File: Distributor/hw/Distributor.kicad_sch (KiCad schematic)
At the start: 23 parts, among them J1 Conn_01x04, J100 Conn_01x03, J2 Conn_01x06_MountingPin, U1 SPX3819M5-L-3-3, U2 STM32G030C8Tx, U3 SN74AHCT245PWR, U4 SN74AHCT245PWR, U5 SN74AHCT245PWR, U6 SN74AHCT245PWR

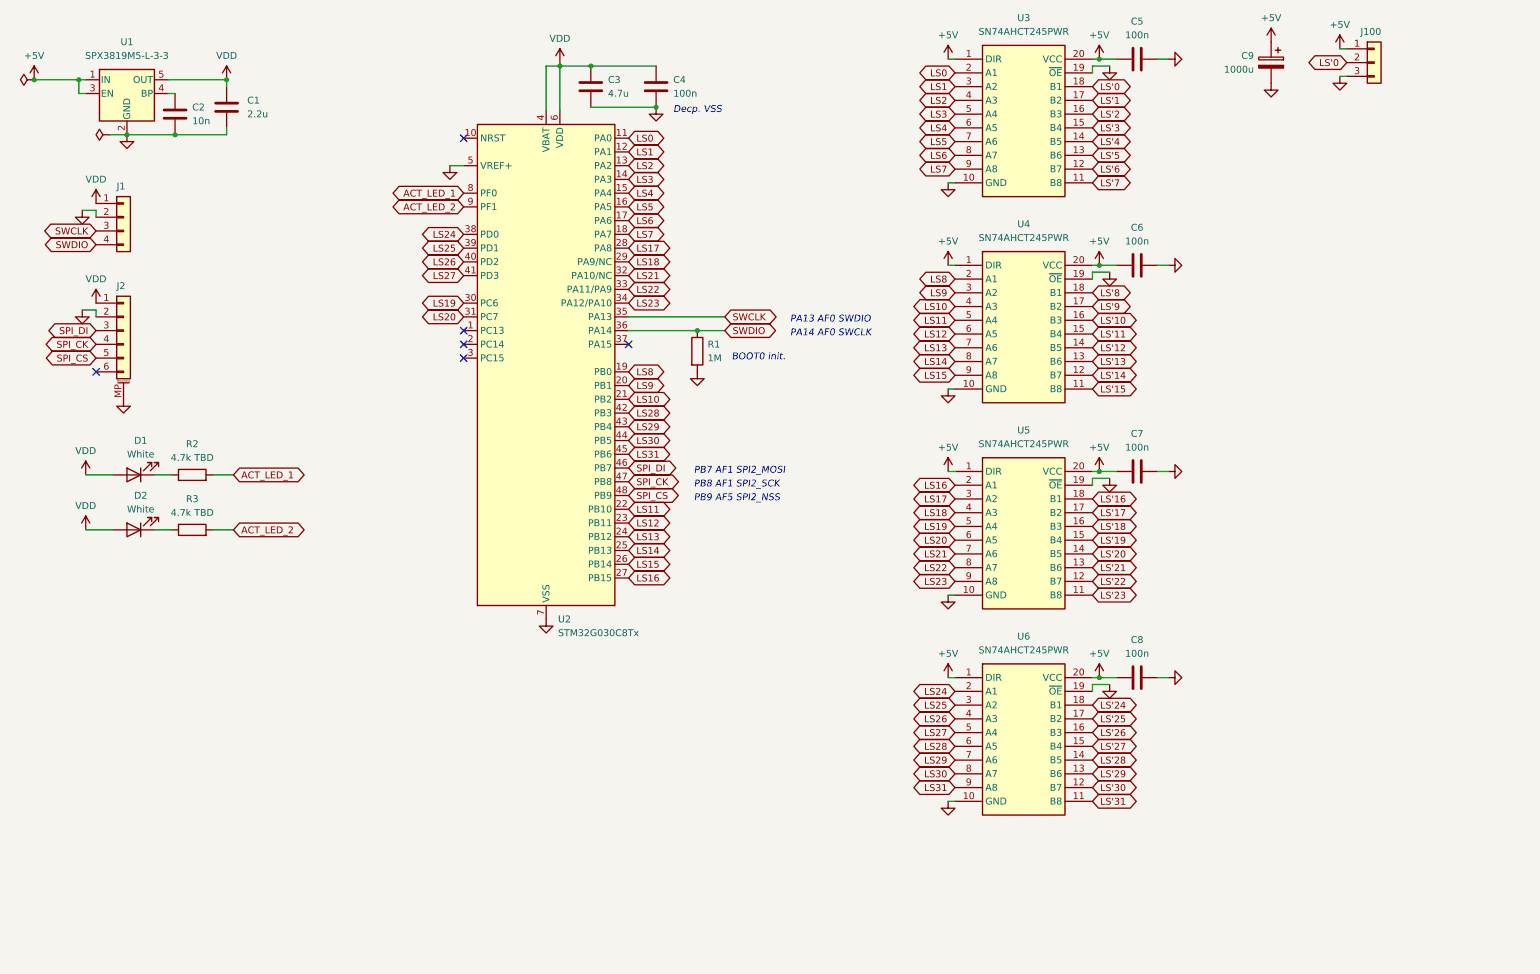
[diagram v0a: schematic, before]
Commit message: Merge distributor and grabber schematic into one
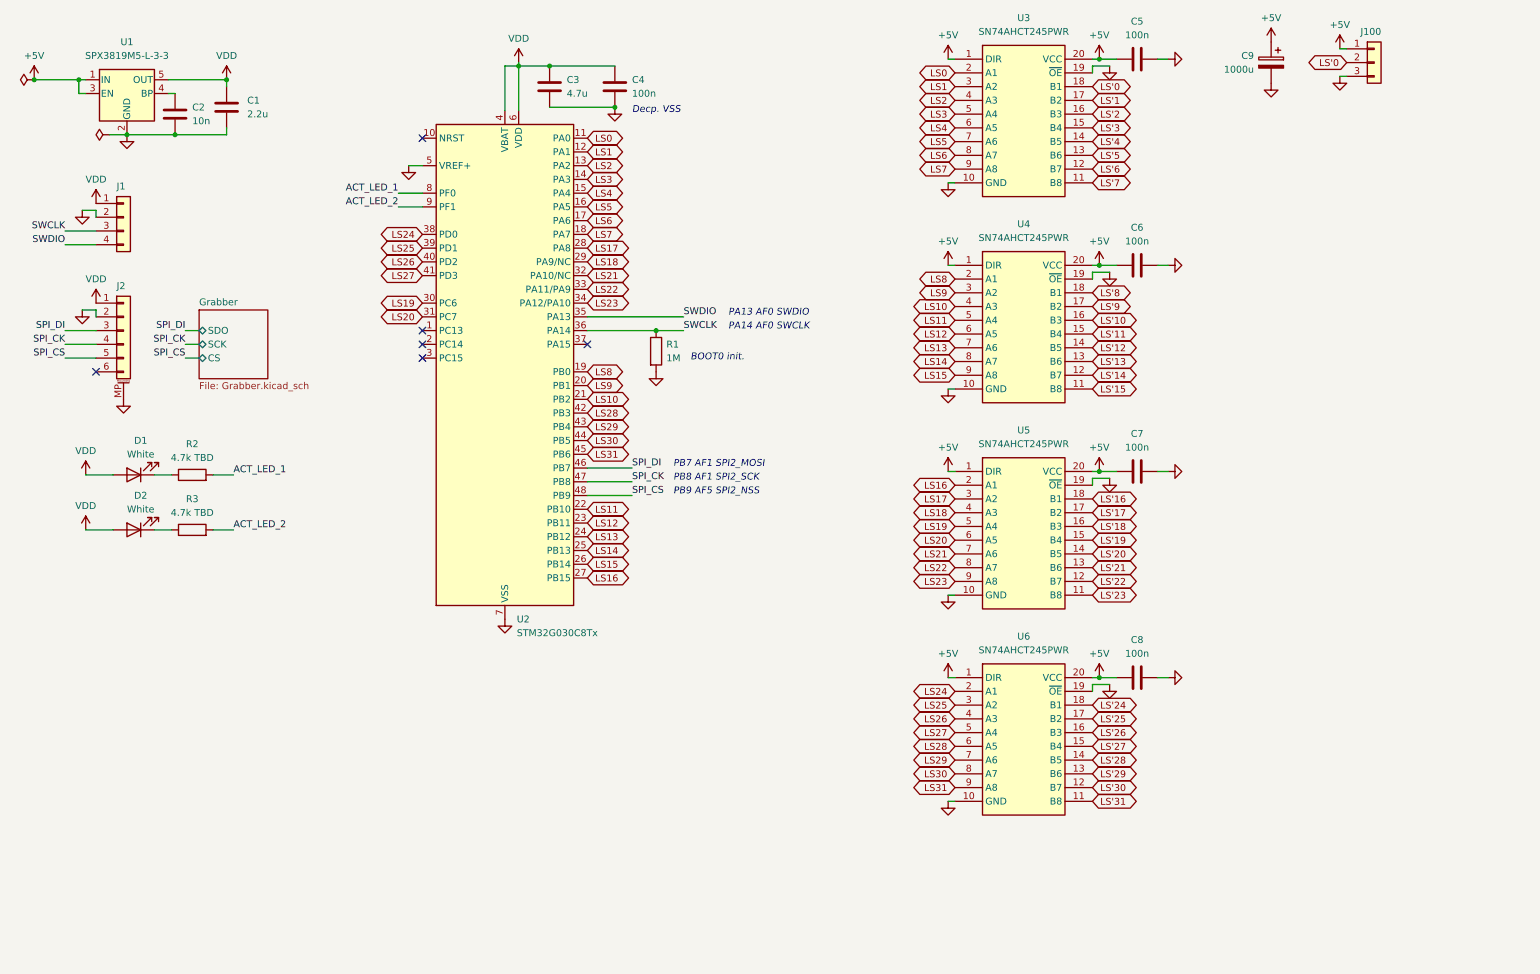
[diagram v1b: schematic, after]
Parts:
- J100: footprint (none) -> Connector_PinHeader_2.54mm:PinHeader_1x03_P2.54mm_Vertical
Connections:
- net SWCLK: now also R1.1, U2.36 (PA14); no longer U2.35 (PA13)
- net SWDIO: now also U2.35 (PA13); no longer R1.1, U2.36 (PA14)
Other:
- added sheet Grabber (Grabber.kicad_sch)
- moved on the sheet: C3, C4, R1, U2

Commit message: Add MLX90640 sensor to schematic
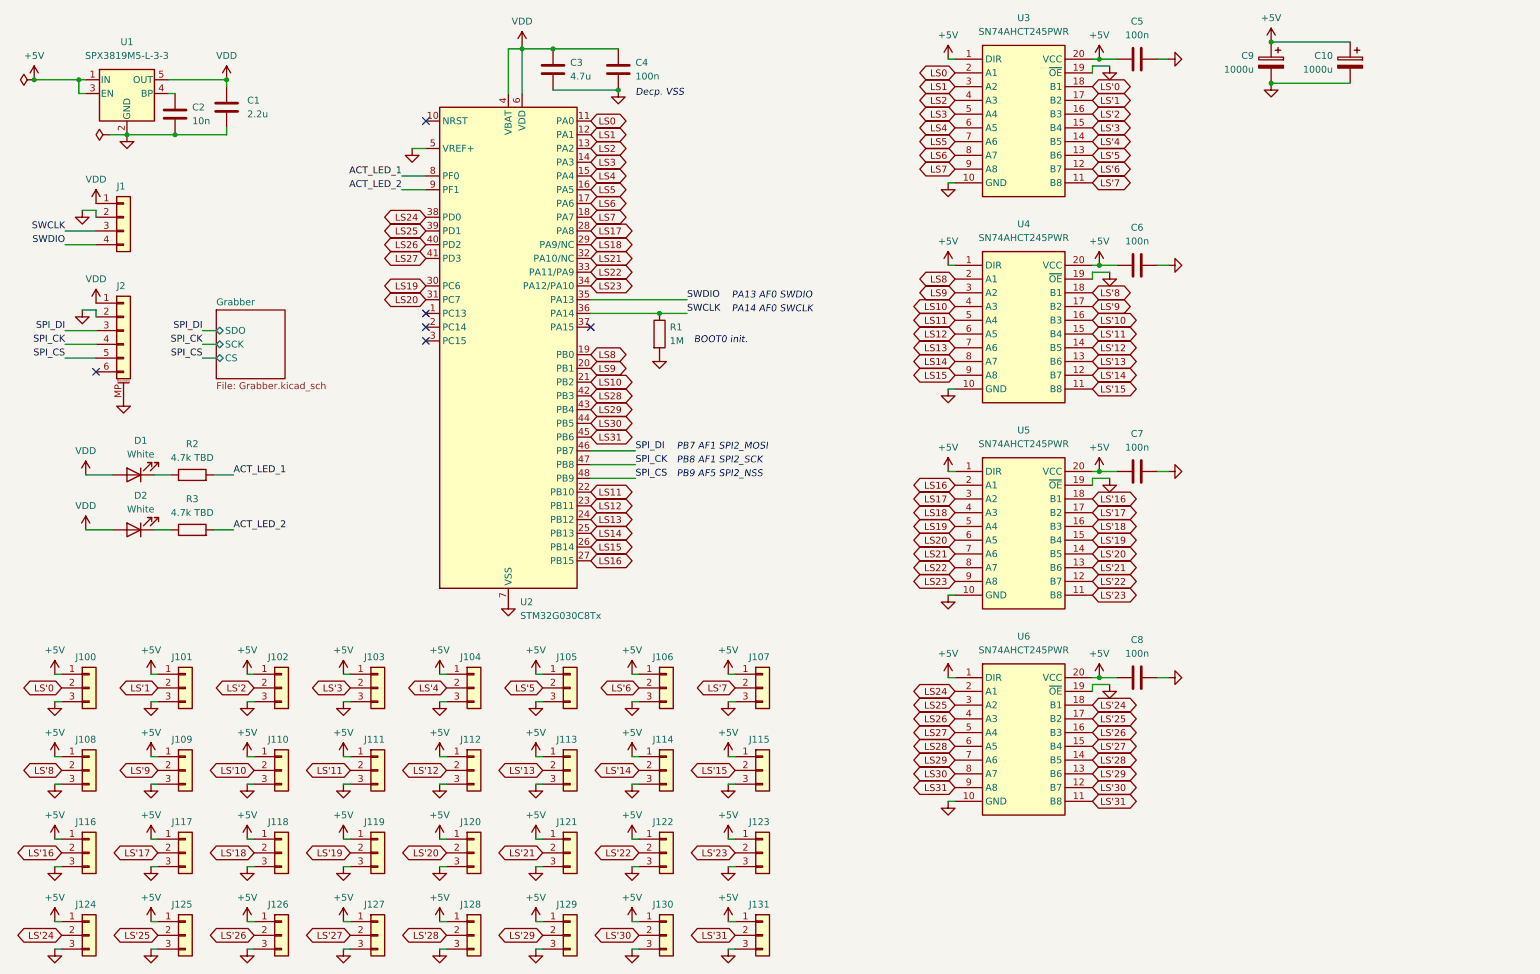
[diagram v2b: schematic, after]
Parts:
- added C10: 1000u, Capacitor_SMD:CP_Elec_8x10.5, symbol Device:C_Polarized
- added J101, J102, J103, J104, J105, J106, J107, J108, J109, J110, J111, J112, J113, J114, J115, J116, J117, J118, J119, J120, J121, J122, J123, J124, J125, J126, J127, J128, J129, J130, J131: Conn_01x03, Distributor_footprints:PinHeader_1x03_P2.54mm_Vertical, symbol Connector_Generic:Conn_01x03
- J100: footprint Connector_PinHeader_2.54mm:PinHeader_1x03_P2.54mm_Vertical -> Distributor_footprints:PinHeader_1x03_P2.54mm_Vertical
- J2: footprint Connector_FFC-FPC:TE_84952-6_1x06-1MP_P1.0mm_Horizontal -> Connector_FFC-FPC:Jushuo_AFC07-S06FCA-00_1x6-1MP_P0.50_Horizontal
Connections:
- net +5V: now also C10.1, J101.1 (Pin_1), J102.1 (Pin_1), J103.1 (Pin_1), J104.1 (Pin_1), J105.1 (Pin_1), J106.1 (Pin_1), J107.1 (Pin_1), J108.1 (Pin_1), J109.1 (Pin_1), J110.1 (Pin_1), J111.1 (Pin_1), J112.1 (Pin_1), J113.1 (Pin_1), J114.1 (Pin_1), J115.1 (Pin_1), J116.1 (Pin_1), J117.1 (Pin_1), J118.1 (Pin_1), J119.1 (Pin_1), J120.1 (Pin_1), J121.1 (Pin_1), J122.1 (Pin_1), J123.1 (Pin_1), J124.1 (Pin_1), J125.1 (Pin_1), J126.1 (Pin_1), J127.1 (Pin_1), J128.1 (Pin_1), J129.1 (Pin_1), J130.1 (Pin_1), J131.1 (Pin_1)
- net GND: now also C10.2, J101.3 (Pin_3), J102.3 (Pin_3), J103.3 (Pin_3), J104.3 (Pin_3), J105.3 (Pin_3), J106.3 (Pin_3), J107.3 (Pin_3), J108.3 (Pin_3), J109.3 (Pin_3), J110.3 (Pin_3), J111.3 (Pin_3), J112.3 (Pin_3), J113.3 (Pin_3), J114.3 (Pin_3), J115.3 (Pin_3), J116.3 (Pin_3), J117.3 (Pin_3), J118.3 (Pin_3), J119.3 (Pin_3), J120.3 (Pin_3), J121.3 (Pin_3), J122.3 (Pin_3), J123.3 (Pin_3), J124.3 (Pin_3), J125.3 (Pin_3), J126.3 (Pin_3), J127.3 (Pin_3), J128.3 (Pin_3), J129.3 (Pin_3), J130.3 (Pin_3), J131.3 (Pin_3)
- net LS'1: now also J101.2 (Pin_2)
- net LS'10: now also J110.2 (Pin_2)
- net LS'11: now also J111.2 (Pin_2)
- net LS'12: now also J112.2 (Pin_2)
- net LS'13: now also J113.2 (Pin_2)
- net LS'14: now also J114.2 (Pin_2)
- net LS'15: now also J115.2 (Pin_2)
- net LS'16: now also J116.2 (Pin_2)
- net LS'17: now also J117.2 (Pin_2)
- net LS'18: now also J118.2 (Pin_2)
- net LS'19: now also J119.2 (Pin_2)
- net LS'2: now also J102.2 (Pin_2)
- net LS'20: now also J120.2 (Pin_2)
- net LS'21: now also J121.2 (Pin_2)
- net LS'22: now also J122.2 (Pin_2)
- net LS'23: now also J123.2 (Pin_2)
- net LS'24: now also J124.2 (Pin_2)
- net LS'25: now also J125.2 (Pin_2)
- net LS'26: now also J126.2 (Pin_2)
- net LS'27: now also J127.2 (Pin_2)
- net LS'28: now also J128.2 (Pin_2)
- net LS'29: now also J129.2 (Pin_2)
- net LS'3: now also J103.2 (Pin_2)
- net LS'30: now also J130.2 (Pin_2)
- net LS'31: now also J131.2 (Pin_2)
- net LS'4: now also J104.2 (Pin_2)
- net LS'5: now also J105.2 (Pin_2)
- net LS'6: now also J106.2 (Pin_2)
- net LS'7: now also J107.2 (Pin_2)
- net LS'8: now also J108.2 (Pin_2)
- net LS'9: now also J109.2 (Pin_2)
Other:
- moved on the sheet: C3, C4, J100, R1, U2

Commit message: Separate 5V power supplies into four domains
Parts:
- added C11, C12: 1000u, Capacitor_SMD:CP_Elec_8x10.5, symbol Device:C_Polarized
- added J3, J4, J5, J6: Conn_01x02, Connector_PinHeader_2.54mm:PinHeader_1x02_P2.54mm_Vertical, symbol Connector_Generic:Conn_01x02
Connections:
- net GND: now also C11.2, C12.2, J3.2 (Pin_2), J4.2 (Pin_2), J5.2 (Pin_2), J6.2 (Pin_2)
- net LS'0: now also U3.11 (B8); no longer U3.18 (B1)
- net LS'1: now also U3.12 (B7); no longer U3.17 (B2)
- net LS'10: now also U4.13 (B6); no longer U4.16 (B3)
- net LS'11: now also U4.14 (B5); no longer U4.15 (B4)
- net LS'12: now also U4.15 (B4); no longer U4.14 (B5)
- net LS'13: now also U4.16 (B3); no longer U4.13 (B6)
- net LS'14: now also U4.17 (B2); no longer U4.12 (B7)
- net LS'15: now also U4.18 (B1); no longer U4.11 (B8)
- net LS'16: now also U5.11 (B8); no longer U5.18 (B1)
- net LS'17: now also U5.12 (B7); no longer U5.17 (B2)
- net LS'18: now also U5.13 (B6); no longer U5.16 (B3)
- net LS'19: now also U5.14 (B5); no longer U5.15 (B4)
- net LS'2: now also U3.13 (B6); no longer U3.16 (B3)
- net LS'20: now also U5.15 (B4); no longer U5.14 (B5)
- net LS'21: now also U5.16 (B3); no longer U5.13 (B6)
- net LS'22: now also U5.17 (B2); no longer U5.12 (B7)
- net LS'23: now also U5.18 (B1); no longer U5.11 (B8)
- net LS'24: now also U6.11 (B8); no longer U6.18 (B1)
- net LS'25: now also U6.12 (B7); no longer U6.17 (B2)
- net LS'26: now also U6.13 (B6); no longer U6.16 (B3)
- net LS'27: now also U6.14 (B5); no longer U6.15 (B4)
- net LS'28: now also U6.15 (B4); no longer U6.14 (B5)
- net LS'29: now also U6.16 (B3); no longer U6.13 (B6)
- net LS'3: now also U3.14 (B5); no longer U3.15 (B4)
- net LS'30: now also U6.17 (B2); no longer U6.12 (B7)
- net LS'31: now also U6.18 (B1); no longer U6.11 (B8)
- net LS'4: now also U3.15 (B4); no longer U3.14 (B5)
- net LS'5: now also U3.16 (B3); no longer U3.13 (B6)
- net LS'6: now also U3.17 (B2); no longer U3.12 (B7)
- net LS'7: now also U3.18 (B1); no longer U3.11 (B8)
- net LS'8: now also U4.11 (B8); no longer U4.18 (B1)
- net LS'9: now also U4.12 (B7); no longer U4.17 (B2)
- net LS0: now also U3.9 (A8); no longer U3.2 (A1)
- net LS1: now also U3.8 (A7); no longer U3.3 (A2)
- net LS10: now also U4.7 (A6); no longer U4.4 (A3)
- net LS11: now also U4.6 (A5); no longer U4.5 (A4)
- net LS12: now also U4.5 (A4); no longer U4.6 (A5)
- net LS13: now also U4.4 (A3); no longer U4.7 (A6)
- net LS14: now also U4.3 (A2); no longer U4.8 (A7)
- net LS15: now also U4.2 (A1); no longer U4.9 (A8)
- net LS16: now also U5.9 (A8); no longer U5.2 (A1)
- net LS17: now also U5.8 (A7); no longer U5.3 (A2)
- net LS18: now also U5.7 (A6); no longer U5.4 (A3)
- net LS19: now also U5.6 (A5); no longer U5.5 (A4)
- net LS2: now also U3.7 (A6); no longer U3.4 (A3)
- net LS20: now also U5.5 (A4); no longer U5.6 (A5)
- net LS21: now also U5.4 (A3); no longer U5.7 (A6)
- net LS22: now also U5.3 (A2); no longer U5.8 (A7)
- net LS23: now also U5.2 (A1); no longer U5.9 (A8)
- net LS24: now also U6.9 (A8); no longer U6.2 (A1)
- net LS25: now also U6.8 (A7); no longer U6.3 (A2)
- net LS26: now also U6.7 (A6); no longer U6.4 (A3)
- net LS27: now also U6.6 (A5); no longer U6.5 (A4)
- net LS28: now also U6.5 (A4); no longer U6.6 (A5)
- net LS29: now also U6.4 (A3); no longer U6.7 (A6)
- net LS3: now also U3.6 (A5); no longer U3.5 (A4)
- net LS30: now also U6.3 (A2); no longer U6.8 (A7)
- net LS31: now also U6.2 (A1); no longer U6.9 (A8)
- net LS4: now also U3.5 (A4); no longer U3.6 (A5)
- net LS5: now also U3.4 (A3); no longer U3.7 (A6)
- net LS6: now also U3.3 (A2); no longer U3.8 (A7)
- net LS7: now also U3.2 (A1); no longer U3.9 (A8)
- net LS8: now also U4.9 (A8); no longer U4.2 (A1)
- net LS9: now also U4.8 (A7); no longer U4.3 (A2)
- removed net +5V: C10.1, C5.1, C6.1, C7.1, C8.1, C9.1, J100.1 (Pin_1), J101.1 (Pin_1), J102.1 (Pin_1), J103.1 (Pin_1), J104.1 (Pin_1), J105.1 (Pin_1), J106.1 (Pin_1), J107.1 (Pin_1), J108.1 (Pin_1), J109.1 (Pin_1), J110.1 (Pin_1), J111.1 (Pin_1), J112.1 (Pin_1), J113.1 (Pin_1), J114.1 (Pin_1), J115.1 (Pin_1), J116.1 (Pin_1), J117.1 (Pin_1), J118.1 (Pin_1), J119.1 (Pin_1), J120.1 (Pin_1), J121.1 (Pin_1), J122.1 (Pin_1), J123.1 (Pin_1), J124.1 (Pin_1), J125.1 (Pin_1), J126.1 (Pin_1), J127.1 (Pin_1), J128.1 (Pin_1), J129.1 (Pin_1), J130.1 (Pin_1), J131.1 (Pin_1), U1.1 (IN), U1.3 (EN), U3.1 (DIR), U3.20 (VCC), U4.1 (DIR), U4.20 (VCC), U5.1 (DIR), U5.20 (VCC), U6.1 (DIR), U6.20 (VCC)
- new net +5V-A: C5.1, C9.1, J100.1 (Pin_1), J101.1 (Pin_1), J102.1 (Pin_1), J103.1 (Pin_1), J104.1 (Pin_1), J105.1 (Pin_1), J106.1 (Pin_1), J107.1 (Pin_1), J3.1 (Pin_1), U3.1 (DIR), U3.20 (VCC)
- new net +5V-B: C10.1, C6.1, J108.1 (Pin_1), J109.1 (Pin_1), J110.1 (Pin_1), J111.1 (Pin_1), J112.1 (Pin_1), J113.1 (Pin_1), J114.1 (Pin_1), J115.1 (Pin_1), J4.1 (Pin_1), U4.1 (DIR), U4.20 (VCC)
- new net +5V-C: C11.1, C7.1, J116.1 (Pin_1), J117.1 (Pin_1), J118.1 (Pin_1), J119.1 (Pin_1), J120.1 (Pin_1), J121.1 (Pin_1), J122.1 (Pin_1), J123.1 (Pin_1), J5.1 (Pin_1), U5.1 (DIR), U5.20 (VCC)
- new net +5V-D: C12.1, C8.1, J124.1 (Pin_1), J125.1 (Pin_1), J126.1 (Pin_1), J127.1 (Pin_1), J128.1 (Pin_1), J129.1 (Pin_1), J130.1 (Pin_1), J131.1 (Pin_1), J6.1 (Pin_1), U1.1 (IN), U1.3 (EN), U6.1 (DIR), U6.20 (VCC)

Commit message: Board layout
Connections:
- net +5V-A: now also U1.1 (IN), U1.3 (EN)
- net +5V-D: no longer U1.1 (IN), U1.3 (EN)
- net GND: no longer U2.5 (VREF+)
- net VDD: now also U2.5 (VREF+)
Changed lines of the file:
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@@
     (stroke (width 0) (type default))
   )
-  (wire (pts (xy 93.98 40.005) (xy 96.52 40.005))
+  (wire (pts (xy 92.71 40.005) (xy 96.52 40.005))
     (stroke (width 0) (type default))
   )
@@
     )
   )
-  (symbol (lib_id "Distributor_symbols:+5V-D") (at 24.13 27.305 0) (unit 1)
-    (in_bom yes) (on_board yes) (dnp no)
-    (property "Reference" "#PWR01" (at 24.13 31.115 0)
-      (effects (font (size 1.27 1.27)) hide)
-    )
-    (property "Value" "+5V-D" (at 24.13 22.86 0)
-      (effects (font (size 1.27 1.27)))
-    )
-    (property "Footprint" "" (at 24.13 27.305 0)
-      (effects (font (size 1.27 1.27)) hide)
-    )
-    (property "Datasheet" "" (at 24.13 27.305 0)
-      (effects (font (size 1.27 1.27)) hide)
-    )
-    (pin "1")
-    (instances
-      (project "Distributor"
-        (path "/3f67d80a-1b5b-4b57-a63e-46eb7de4787a"
-          (reference "#PWR01") (unit 1)
-        )
-      )
-    )
-  )
   (symbol (lib_id "power:GND") (at 278.13 43.815 0) (unit 1)
     (in_bom yes) (on_board yes) (dnp no) (fields_autoplaced)
@@
     )
   )
-  (symbol (lib_id "power:GND") (at 93.98 40.005 0) (unit 1)
-    (in_bom yes) (on_board yes) (dnp no) (fields_autoplaced)
-    (property "Reference" "#PWR09" (at 93.98 46.355 0)
-      (effects (font (size 1.27 1.27)) hide)
-    )
-    (property "Value" "GND" (at 93.98 44.45 0)
-      (effects (font (size 1.27 1.27)) hide)
-    )
-    (property "Footprint" "" (at 93.98 40.005 0)
-      (effects (font (size 1.27 1.27)) hide)
-    )
-    (property "Datasheet" "" (at 93.98 40.005 0)
-      (effects (font (size 1.27 1.27)) hide)
-    )
-    (pin "1")
-    (instances
-      (project "Distributor"
-        (path "/3f67d80a-1b5b-4b57-a63e-46eb7de4787a"
-          (reference "#PWR09") (unit 1)
-        )
-      )
-    )
-  )
   (symbol (lib_id "Device:C") (at 227.965 137.795 90) (unit 1)
     (in_bom yes) (on_board yes) (dnp no)
@@
     )
   )
+  (symbol (lib_id "power:VDD") (at 92.71 40.005 0) (unit 1)
+    (in_bom yes) (on_board yes) (dnp no) (fields_autoplaced)
+    (property "Reference" "#PWR09" (at 92.71 43.815 0)
+      (effects (font (size 1.27 1.27)) hide)
+    )
+    (property "Value" "VDD" (at 92.71 35.56 0)
+      (effects (font (size 1.27 1.27)))
+    )
+    (property "Footprint" "" (at 92.71 40.005 0)
+      (effects (font (size 1.27 1.27)) hide)
+    )
+    (property "Datasheet" "" (at 92.71 40.005 0)
+      (effects (font (size 1.27 1.27)) hide)
+    )
+    (pin "1")
+    (instances
+      (project "Distributor"
+        (path "/3f67d80a-1b5b-4b57-a63e-46eb7de4787a"
+          (reference "#PWR09") (unit 1)
+        )
+      )
+    )
+  )
   (symbol (lib_id "Distributor_symbols:+5V-B") (at 267.335 20.32 0) (unit 1)
     (in_bom yes) (on_board yes) (dnp no) (fields_autoplaced)
@@
         )
       )
+    )
+  )
+  (symbol (lib_id "Distributor_symbols:+5V-A") (at 24.13 27.305 0) (unit 1)
+    (in_bom yes) (on_board yes) (dnp no) (fields_autoplaced)
+    (property "Reference" "#PWR01" (at 24.13 31.115 0)
+      (effects (font (size 1.27 1.27)) hide)
+    )
+    (property "Value" "+5V-A" (at 24.13 22.86 0)
+      (effects (font (size 1.27 1.27)))
+    )
+    (property "Footprint" "" (at 24.13 27.305 0)
+      (effects (font (size 1.27 1.27)) hide)
+    )
+    (property "Datasheet" "" (at 24.13 27.305 0)
+      (effects (font (size 1.27 1.27)) hide)
+    )
+    (pin "1")
+    (instances
+      (project "Distributor"
+        (path "/3f67d80a-1b5b-4b57-a63e-46eb7de4787a"
+          (reference "#PWR01") (unit 1)
+        )
+      )
